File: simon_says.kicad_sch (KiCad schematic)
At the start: 14 parts, among them SW1 SW_Push_LED, SW2 SW_Push_LED, SW3 SW_Push_LED, SW4 SW_Push_LED, U1 ATtiny25-20P

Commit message: First take on component placement
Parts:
- D1, D2, D3, D4: footprint Diode_THT:D_DO-41_SOD81_P10.16mm_Horizontal -> Diode_THT:D_DO-34_SOD68_P7.62mm_Horizontal
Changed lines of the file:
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@@
       (effects (font (size 1.27 1.27)) (justify right))
     )
-    (property "Footprint" "Diode_THT:D_DO-41_SOD81_P10.16mm_Horizontal" (at 159.385 59.69 0)
+    (property "Footprint" "Diode_THT:D_DO-34_SOD68_P7.62mm_Horizontal" (at 159.385 59.69 0)
       (effects (font (size 1.27 1.27)) hide)
     )
@@
       (effects (font (size 1.27 1.27)) (justify right))
     )
-    (property "Footprint" "Diode_THT:D_DO-41_SOD81_P10.16mm_Horizontal" (at 116.205 59.69 0)
+    (property "Footprint" "Diode_THT:D_DO-34_SOD68_P7.62mm_Horizontal" (at 116.205 59.69 0)
       (effects (font (size 1.27 1.27)) hide)
     )
@@
       (effects (font (size 1.27 1.27)) (justify right))
     )
-    (property "Footprint" "Diode_THT:D_DO-41_SOD81_P10.16mm_Horizontal" (at 182.245 59.69 0)
+    (property "Footprint" "Diode_THT:D_DO-34_SOD68_P7.62mm_Horizontal" (at 182.245 59.69 0)
       (effects (font (size 1.27 1.27)) hide)
     )
@@
       (effects (font (size 1.27 1.27)) (justify right))
     )
-    (property "Footprint" "Diode_THT:D_DO-41_SOD81_P10.16mm_Horizontal" (at 139.065 59.69 0)
-      (effects (font (size 1.27 1.27)) hide)
-    )
+    (property "Footprint" "Diode_THT:D_DO-34_SOD68_P7.62mm_Horizontal" (at 139.065 59.69 0)
+      (effects (font (size 1.27 1.27)) hide)
+    )

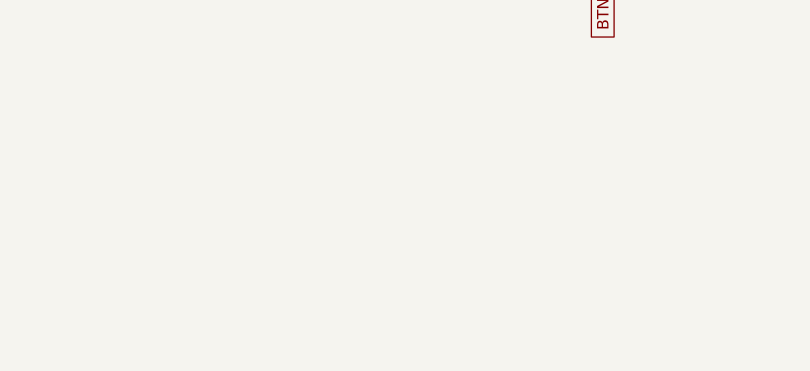
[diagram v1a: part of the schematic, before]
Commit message: Added speaker
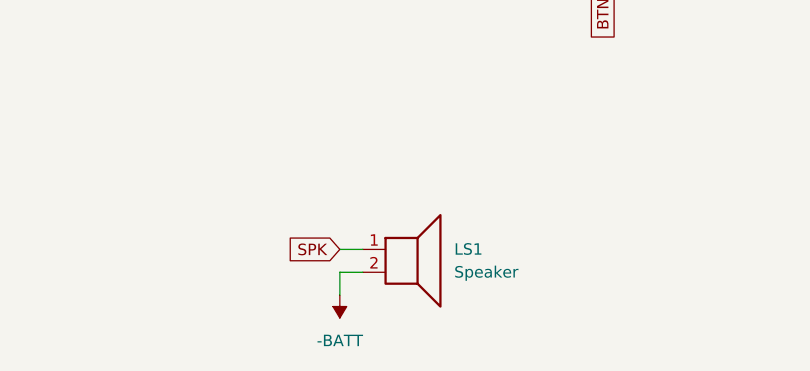
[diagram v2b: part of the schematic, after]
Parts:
- added LS1: Speaker, Connector_PinHeader_2.54mm:PinHeader_1x02_P2.54mm_Vertical, symbol Device:Speaker
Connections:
- net -BATT: now also LS1.2
- net SPK: now also LS1.1
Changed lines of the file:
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@@
+    (stroke (width 0) (type default))
+  )
+  (wire (pts (xy 119.38 101.6) (xy 116.84 101.6))
     (stroke (width 0) (type default))
   )
@@
     (stroke (width 0) (type default))
   )
+  (wire (pts (xy 116.84 99.06) (xy 119.38 99.06))
+    (stroke (width 0) (type default))
+  )
   (wire (pts (xy 224.79 57.15) (xy 224.79 68.58))
     (stroke (width 0) (type default))
@@
   )
   (wire (pts (xy 114.3 41.91) (xy 114.3 38.1))
+    (stroke (width 0) (type default))
+  )
+  (wire (pts (xy 116.84 101.6) (xy 116.84 104.14))
     (stroke (width 0) (type default))
   )
@@
     (property "Intersheetrefs" "${INTERSHEET_REFS}" (at 177.8 20.8425 90)
       (effects (font (size 1.27 1.27)) (justify left) hide)
+    )
+  )
+  (global_label "SPK" (shape input) (at 116.84 99.06 180) (fields_autoplaced)
+    (effects (font (size 1.27 1.27)) (justify right))
+    (property "Intersheetrefs" "${INTERSHEET_REFS}" (at 110.1053 99.06 0)
+      (effects (font (size 1.27 1.27)) (justify right) hide)
     )
   )
@@
     )
   )
+  (symbol (lib_id "Device:Speaker") (at 124.46 99.06 0) (unit 1)
+    (in_bom yes) (on_board yes) (dnp no) (fields_autoplaced)
+    (property "Reference" "LS1" (at 129.54 99.06 0)
+      (effects (font (size 1.27 1.27)) (justify left))
+    )
+    (property "Value" "Speaker" (at 129.54 101.6 0)
+      (effects (font (size 1.27 1.27)) (justify left))
+    )
+    (property "Footprint" "Connector_PinHeader_2.54mm:PinHeader_1x02_P2.54mm_Vertical" (at 124.46 104.14 0)
+      (effects (font (size 1.27 1.27)) hide)
+    )
+    (property "Datasheet" "~" (at 124.206 100.33 0)
+      (effects (font (size 1.27 1.27)) hide)
+    )
+    (pin "1")
+    (pin "2")
+    (instances
+      (project "simon_says"
+        (path "/db54bf83-09f4-46d1-a2eb-9b287b3cc432"
+          (reference "LS1") (unit 1)
+        )
+      )
+    )
+  )
   (symbol (lib_id "Device:LED") (at 224.79 53.34 90) (unit 1)
     (in_bom yes) (on_board yes) (dnp no) (fields_autoplaced)
@@
         )
       )
+    )
+  )
+  (symbol (lib_id "power:-BATT") (at 116.84 104.14 180) (unit 1)
+    (in_bom yes) (on_board yes) (dnp no) (fields_autoplaced)
+    (property "Reference" "#PWR03" (at 116.84 100.33 0)
+      (effects (font (size 1.27 1.27)) hide)
+    )
+    (property "Value" "-BATT" (at 116.84 109.22 0)
+      (effects (font (size 1.27 1.27)))
+    )
+    (property "Footprint" "" (at 116.84 104.14 0)
+      (effects (font (size 1.27 1.27)) hide)
+    )
+    (property "Datasheet" "" (at 116.84 104.14 0)
+      (effects (font (size 1.27 1.27)) hide)
+    )
+    (pin "1")
+    (instances
+      (project "simon_says"
+        (path "/db54bf83-09f4-46d1-a2eb-9b287b3cc432"
+          (reference "#PWR03") (unit 1)
+        )
+      )

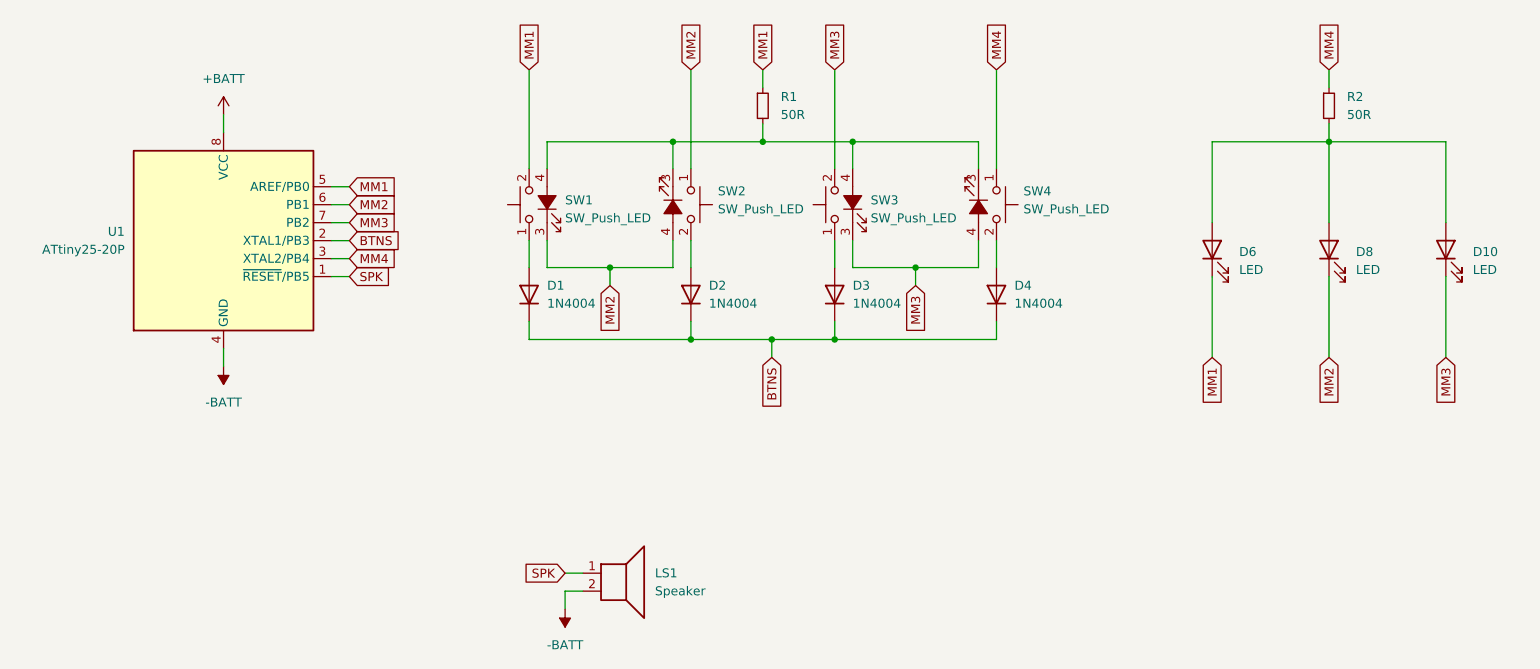
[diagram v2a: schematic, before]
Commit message: Added CR battery pads and removed redundant LEDs
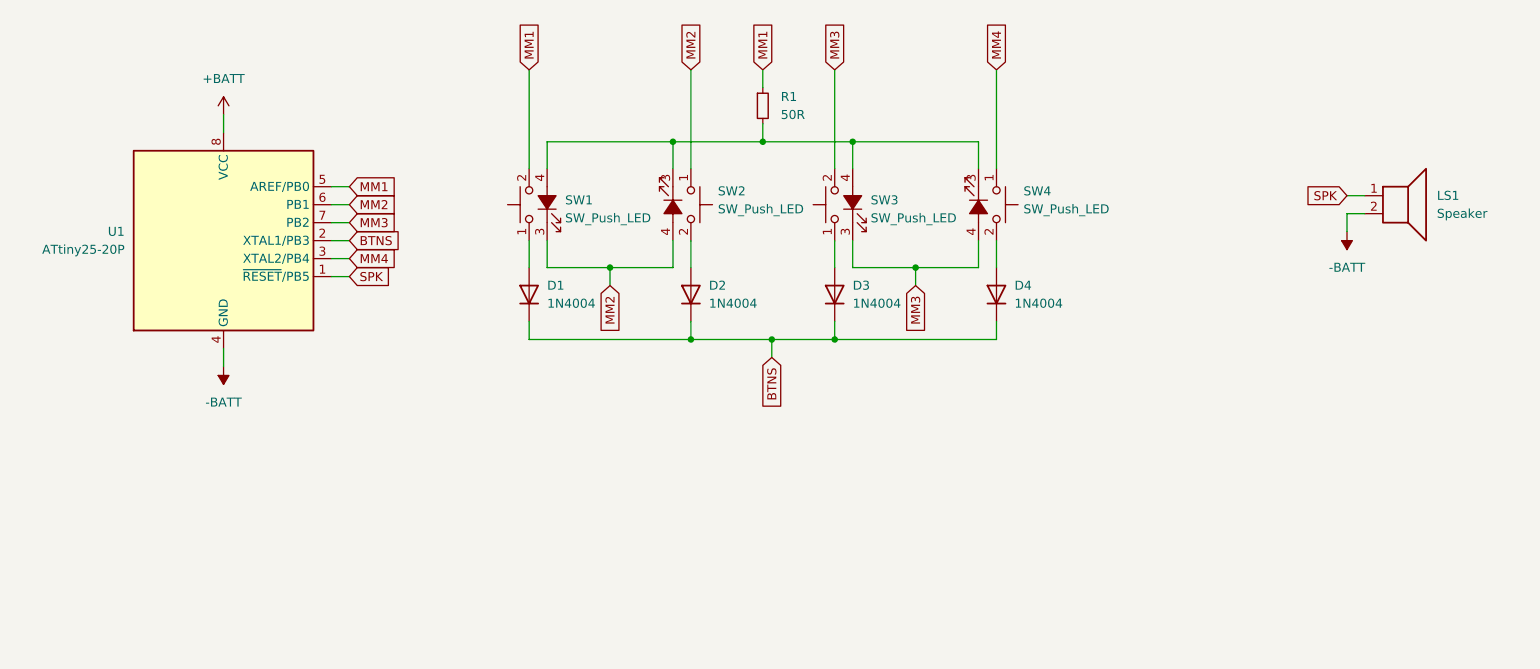
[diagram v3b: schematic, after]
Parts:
- removed D10, D6, D8: LED, LED_THT:LED_D1.8mm_W3.3mm_H2.4mm, symbol Device:LED
- removed R2: 50R, Resistor_THT:R_Axial_DIN0207_L6.3mm_D2.5mm_P7.62mm_Horizontal, symbol Device:R_Small
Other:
- moved on the sheet: LS1

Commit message: The great remake! - added decoupling capacitor - replaced speaker with piezo - added 2450 cell holder - added extra button - rerouted all traces
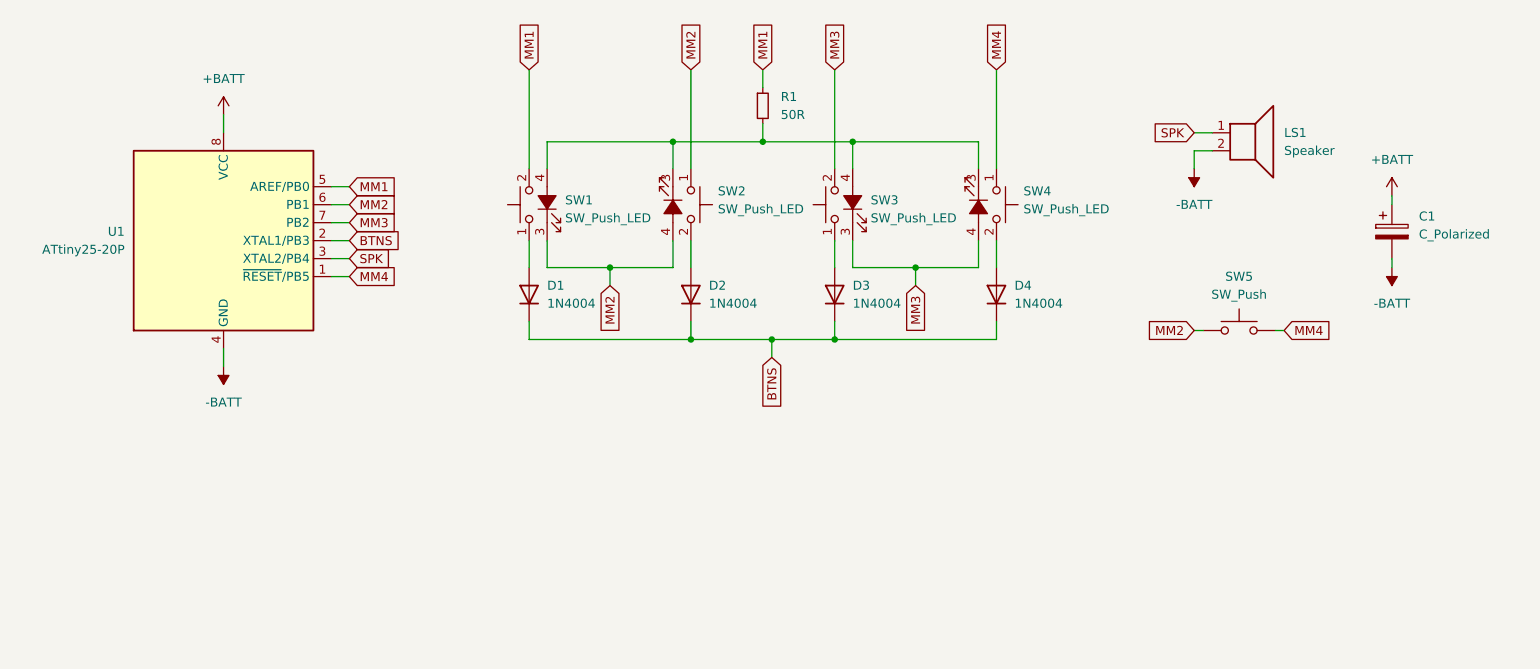
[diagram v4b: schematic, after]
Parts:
- added C1: C_Polarized, symbol Device:C_Polarized
- added SW5: SW_Push, Button_Switch_SMD:SW_MEC_5GSH9, symbol Switch:SW_Push
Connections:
- net +BATT: now also C1.1
- net -BATT: now also C1.2
- net MM2: now also SW5.1
- net MM4: now also U1.1 (~{RESET}/PB5), SW5.2; no longer U1.3 (XTAL2/PB4)
- net SPK: now also U1.3 (XTAL2/PB4); no longer U1.1 (~{RESET}/PB5)
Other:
- moved on the sheet: LS1

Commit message: Improved schematic and pcb: - added real HW reset - avoid using reset pin for IO - reroute all traces
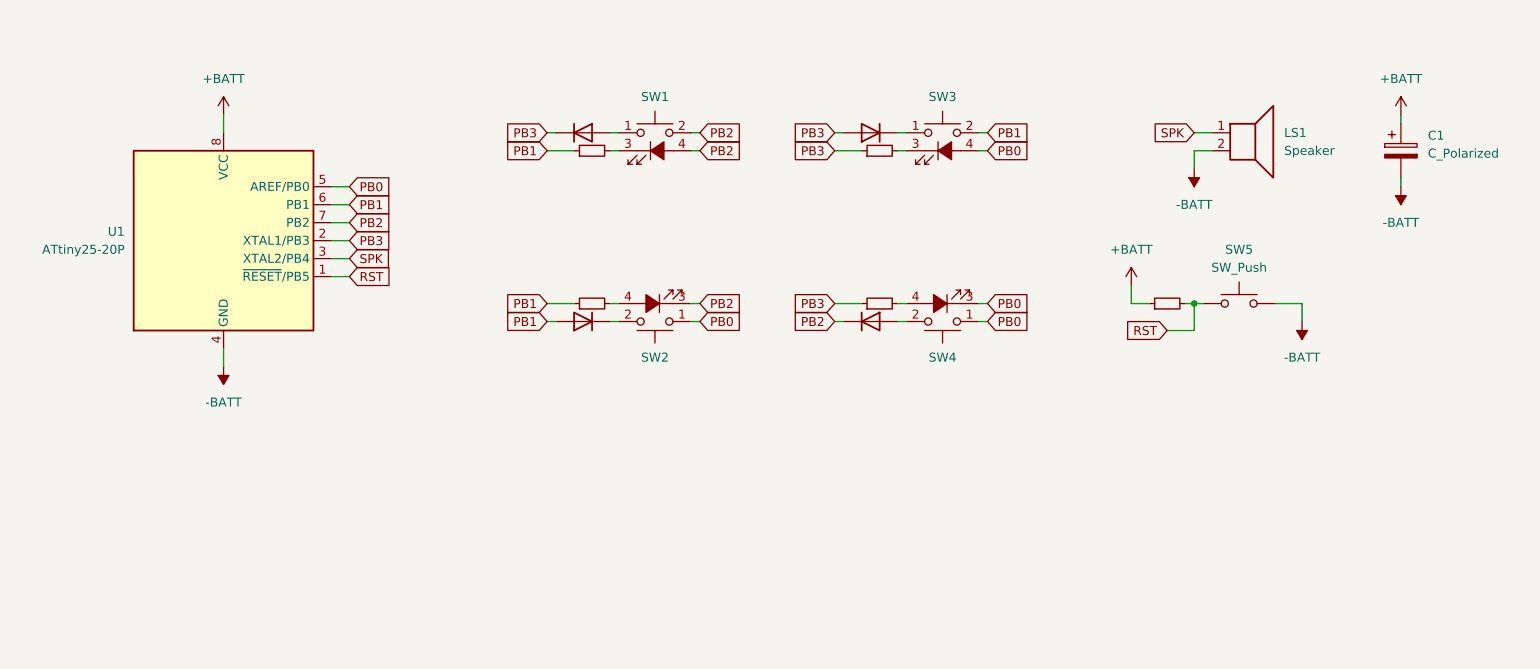
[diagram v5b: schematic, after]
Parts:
- added R2, R3, R4, R5: 50R, Resistor_THT:R_Axial_DIN0207_L6.3mm_D2.5mm_P7.62mm_Horizontal, symbol Device:R_Small
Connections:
- net +BATT: now also R5.1
- net -BATT: now also SW5.2
- net at SW3.1: now also D2.1 (K); no longer D3.2 (A)
- net at SW2.2: now also D3.1 (K); no longer D2.2 (A)
- removed net BTNS: D1.1 (K), D2.1 (K), D3.1 (K), D4.1 (K), U1.2 (XTAL1/PB3)
- removed net MM1: R1.1, SW1.2, U1.5 (AREF/PB0)
- removed net MM2: SW1.3 (K), SW2.1, SW2.4 (A), SW5.1, U1.6 (PB1)
- removed net MM3: SW3.2, SW3.3 (K), SW4.4 (A), U1.7 (PB2)
- removed net MM4: SW4.1, SW5.2, U1.1 (~{RESET}/PB5)
- new net: R1.2, SW3.3 (K)
- new net: R4.2, SW4.4 (A)
- new net: R2.2, SW1.3 (K)
- new net: R3.2, SW2.4 (A)
- new net PB0: SW2.1, SW3.4 (A), SW4.1, SW4.3 (K), U1.5 (AREF/PB0)
- new net PB1: D3.2 (A), R2.1, R3.1, SW3.2, U1.6 (PB1)
- new net PB2: D4.1 (K), SW1.2, SW1.4 (A), SW2.3 (K), U1.7 (PB2)
- new net PB3: D1.1 (K), D2.2 (A), R1.1, R4.1, U1.2 (XTAL1/PB3)
- new net RST: R5.2, SW5.1, U1.1 (~{RESET}/PB5)
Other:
- moved on the sheet: C1, SW1, SW2, SW3, SW4, SW5
